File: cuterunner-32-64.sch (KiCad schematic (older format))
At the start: 39 parts

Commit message: Microcontroller part
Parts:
- added J?: Conn_02x06_Row_Letter_Last, symbol Connector_Generic:Conn_02x06_Row_Letter_Last
- added J?: Conn_01x05, symbol Connector_Generic:Conn_01x05
- C?: value C -> 0.1uF
- R?: value R -> 10k
- R?: value R -> 1k
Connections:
- net labels added: IFACE0, IFACE1, IFACE2, IFACE3, IFACE4, IFACE5, IFACE6, IFACE7, IFACE_CTRL0, IFACE_CTRL1, IFACE_CTRL2, IFACE_CTRL3, TCK_SWCLK, TDI_SWDIO, TDO, TMS_~RST, USB_N, USB_P
- wire segments 13 -> 44
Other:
- moved on the sheet: C?, R?

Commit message: Many CPLD parts
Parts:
- removed D? (x7): LED, symbol Device:LED
- removed R? (x10): R, symbol Device:R
- removed SW? (x3): SW_Push_Dual, symbol Switch:SW_Push_Dual
- added D? (x7): LED, symbol Device:LED
- added J? (x2): Conn_Coaxial, symbol Connector:Conn_Coaxial
- added J? (x2): Conn_01x03, symbol Connector_Generic:Conn_01x03
- added R? (x3): 10k, symbol Device:R
- added R? (x7): 1k, symbol Device:R
- added SW? (x3): SW_Push_Dual, symbol Switch:SW_Push_Dual
- C? (x4): value C -> 0.1uF
- R?: value R -> 1k
- R?: value R -> 10k
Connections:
- net labels added: BUT0, BUT1, BUT2, BUT3, CLK0, CLK1, CLK2, LED4, LED5, LED6, LED7, PMOD0, PMOD1, PMOD2, PMOD3, PMOD4, PMOD5, PMOD6, PMOD7
- wire segments 44 -> 173
- no-connect marks 1 -> 3
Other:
- moved on the sheet: C?, D?, J?, R?, SW?

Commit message: Added osc
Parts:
- added C?: 0.1uF, symbol Device:C
- added U?: OSC, symbol azonenberg-osc:OSC
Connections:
- wire segments 173 -> 178
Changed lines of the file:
@@
 Text Label 12250 4700 0    50   ~ 0
 CLK2
+$Comp
+L azonenberg-osc:OSC U?
+U 1 1 5E192FE7
+P 8600 4300
+F 0 "U?" H 8575 4587 60  0000 C CNN
+F 1 "OSC" H 8575 4481 60  0000 C CNN
+F 2 "" H 8600 4300 60  0000 C CNN
+F 3 "" H 8600 4300 60  0000 C CNN
+	1    8600 4300
+	1    0    0    -1
+$EndComp
+$Comp
+L Device:C C?
+U 1 1 5E193E24
+P 7600 4450
+F 0 "C?" H 7486 4404 50  0000 R CNN
+F 1 "0.1uF" H 7486 4495 50  0000 R CNN
+F 2 "" H 7638 4300 50  0001 C CNN
+F 3 "~" H 7600 4450 50  0001 C CNN
+	1    7600 4450
+	1    0    0    1
+$EndComp
+$Comp
+L power:+3V3 #PWR?
+U 1 1 5E19481A
+P 7600 4300
+F 0 "#PWR?" H 7600 4150 50  0001 C CNN
+F 1 "+3V3" H 7615 4473 50  0000 C CNN
+F 2 "" H 7600 4300 50  0001 C CNN
+F 3 "" H 7600 4300 50  0001 C CNN
+	1    7600 4300
+	1    0    0    -1
+$EndComp
+$Comp
+L power:GND #PWR?
+U 1 1 5E1951AF
+P 7600 4600
+F 0 "#PWR?" H 7600 4350 50  0001 C CNN
+F 1 "GND" H 7605 4427 50  0000 C CNN
+F 2 "" H 7600 4600 50  0001 C CNN
+F 3 "" H 7600 4600 50  0001 C CNN
+	1    7600 4600
+	1    0    0    -1
+$EndComp
+Wire Wire Line
+	7900 4500 7900 4600
+Wire Wire Line
+	7900 4600 7600 4600
+Connection ~ 7600 4600
+Wire Wire Line
+	7900 4400 7900 4300
+Wire Wire Line
+	7900 4300 7600 4300
+Connection ~ 7900 4300
+Connection ~ 7600 4300
+Wire Wire Line
+	9250 4300 9600 4300
+Text Label 9350 4300 0    50   ~ 0
+CLK0
 $EndSCHEMATC

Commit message: Schematic mostly done
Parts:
- added TP1: TestPoint, symbol Connector:TestPoint
- U5: renamed from U?; value OSC -> 50 MHz
- gave numbers to parts that had none: 46
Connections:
- wire segments 178 -> 179
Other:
- note added: "CPLD"
- note added: "Extra global clocks\n\nIntended use: populate only SMA *or* pin headers but not both"
- note added: "MCU programming/debug interface\n\nShares pins with CPLD JTAG, be careful"
- note added: "PMOD expansion (four pins shared with LEDs)"
- note added: "Power supplies"
- note added: "USB interface microcontroller\n\nIntended to be a parallel FIFO or UART interface to CPLD in addition to JTAG programming"
- note added: "User LEDs (four LEDs shared with PMOD)"
- note added: "User pushbuttons"
- moved on the sheet: C1, C2, C3, C4, C5, C6, C7, C8, C9, D1, D2, D3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

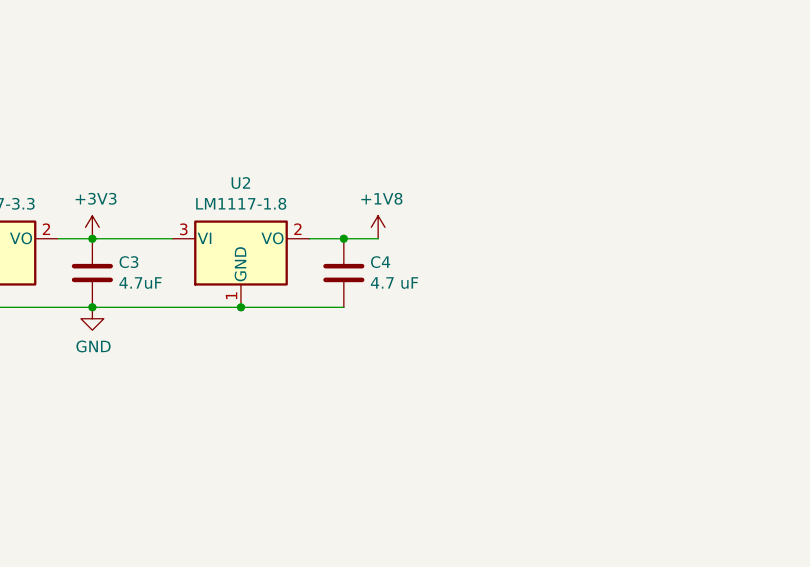
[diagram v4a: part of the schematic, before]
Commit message: Assign footprints
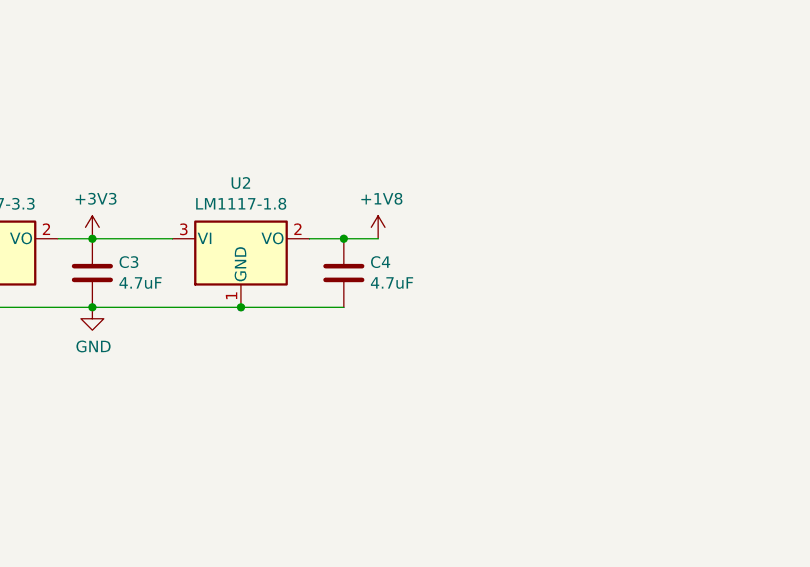
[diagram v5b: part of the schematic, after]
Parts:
- C1, C3: footprint (none) -> Capacitor_SMD:C_1206_3216Metric_Pad1.42x1.75mm_HandSolder
- C2, C5, C6, C7, C8, C9: footprint (none) -> Capacitor_SMD:C_0805_2012Metric_Pad1.15x1.40mm_HandSolder
- C4: value 4.7 uF -> 4.7uF; footprint (none) -> Capacitor_SMD:C_1206_3216Metric_Pad1.42x1.75mm_HandSolder
- D1, D2, D3, D4, D5, D6, D7, D8: footprint (none) -> LED_SMD:LED_0805_2012Metric_Pad1.15x1.40mm_HandSolder
- J1: footprint (none) -> Connector_PinHeader_2.54mm:PinHeader_1x05_P2.54mm_Vertical
- J2: footprint (none) -> Connector_PinHeader_2.54mm:PinHeader_2x06_P2.54mm_Horizontal
- J3, J5: footprint (none) -> azonenberg:CONN_SMA_PTH
- J4, J6: footprint (none) -> Connector_PinHeader_2.54mm:PinHeader_1x03_P2.54mm_Vertical
- R1, R10, R11, R12, R13, R14, R2, R3, R4, R5, R6, R7, R8, R9: footprint (none) -> Resistor_SMD:R_0805_2012Metric_Pad1.15x1.40mm_HandSolder
- SW1, SW2, SW3, SW4: footprint (none) -> Button_Switch_THT:SW_TH_Tactile_Omron_B3F-10xx
- TP1: footprint (none) -> Connector_PinHeader_2.54mm:PinHeader_1x01_P2.54mm_Vertical
- U1, U2: footprint (none) -> Package_TO_SOT_SMD:SOT-223-3_TabPin2
- U4: footprint (none) -> azonenberg:QFP_44_0.8MM
- U5: footprint (none) -> azonenberg:OSCILLATOR_3.2x2.5
- USB1: footprint (none) -> rqou:USB-MICRO-AB

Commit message: Placement of components
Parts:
- removed J2: Conn_02x06_Row_Letter_Last, Connector_PinHeader_2.54mm:PinHeader_2x06_P2.54mm_Horizontal, symbol Connector_Generic:Conn_02x06_Row_Letter_Last
- added J2: Conn_02x06_Odd_Even, Connector_PinHeader_2.54mm:PinHeader_2x06_P2.54mm_Horizontal, symbol Connector_Generic:Conn_02x06_Odd_Even
- added R15: 22, Resistor_SMD:R_0805_2012Metric_Pad1.15x1.40mm_HandSolder, symbol Device:R
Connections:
- wire segments 179 -> 180
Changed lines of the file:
@@
-	1    0    0    -1
-$EndComp
-$Comp
-L Connector_Generic:Conn_02x06_Row_Letter_Last J2
-U 1 1 5DFA98DA
-P 9600 9800
-F 0 "J2" H 9650 10217 50  0000 C CNN
-F 1 "Conn_02x06_Row_Letter_Last" H 9650 10126 50  0000 C CNN
-F 2 "Connector_PinHeader_2.54mm:PinHeader_2x06_P2.54mm_Horizontal" H 9600 9800 50  0001 C CNN
-F 3 "~" H 9600 9800 50  0001 C CNN
-	1    9600 9800
 	1    0    0    -1
 $EndComp
@@
 $EndComp
 Wire Wire Line
-	9400 10100 9900 10100
-Wire Wire Line
-	9900 10100 10000 10100
-Wire Wire Line
 	10000 10100 10000 9400
-Connection ~ 9900 10100
-Wire Wire Line
-	9900 10000 9400 10000
-Wire Wire Line
-	9400 10000 9300 10000
 Wire Wire Line
 	9300 10000 9300 10350
-Connection ~ 9400 10000
 Wire Wire Line
 	11400 6300 12050 6300
@@
 Connection ~ 12600 2100
 Connection ~ 12300 2100
-Wire Wire Line
-	13950 2100 14300 2100
-Text Label 14050 2100 0    50   ~ 0
+Text Label 14550 2100 0    50   ~ 0
 CLK0
 Wire Notes Line
@@
 Text Notes 550  600  0    50   ~ 0
 Power supplies
+$Comp
+L Device:R R15
+U 1 1 5DFC2966
+P 14200 2100
+F 0 "R15" V 13993 2100 50  0000 C CNN
+F 1 "22" V 14084 2100 50  0000 C CNN
+F 2 "Resistor_SMD:R_0805_2012Metric_Pad1.15x1.40mm_HandSolder" V 14130 2100 50  0001 C CNN
+F 3 "~" H 14200 2100 50  0001 C CNN
+	1    14200 2100
+	0    1    1    0
+$EndComp
+$Comp
+L Connector_Generic:Conn_02x06_Odd_Even J2
+U 1 1 5DFC5171
+P 9600 9800
+F 0 "J2" H 9650 10217 50  0000 C CNN
+F 1 "Conn_02x06_Odd_Even" H 9650 10126 50  0000 C CNN
+F 2 "Connector_PinHeader_2.54mm:PinHeader_2x06_P2.54mm_Horizontal" H 9600 9800 50  0001 C CNN
+F 3 "~" H 9600 9800 50  0001 C CNN
+	1    9600 9800
+	1    0    0    -1
+$EndComp
+Wire Wire Line
+	9300 10000 9400 10000
+Wire Wire Line
+	9900 10100 10000 10100
+Wire Wire Line
+	13950 2100 14050 2100
+Wire Wire Line
+	14350 2100 14850 2100
+Wire Wire Line
+	9900 10000 9400 10000
+Connection ~ 9400 10000
+Wire Wire Line
+	9400 10100 9900 10100
+Connection ~ 9900 10100
 $EndSCHEMATC

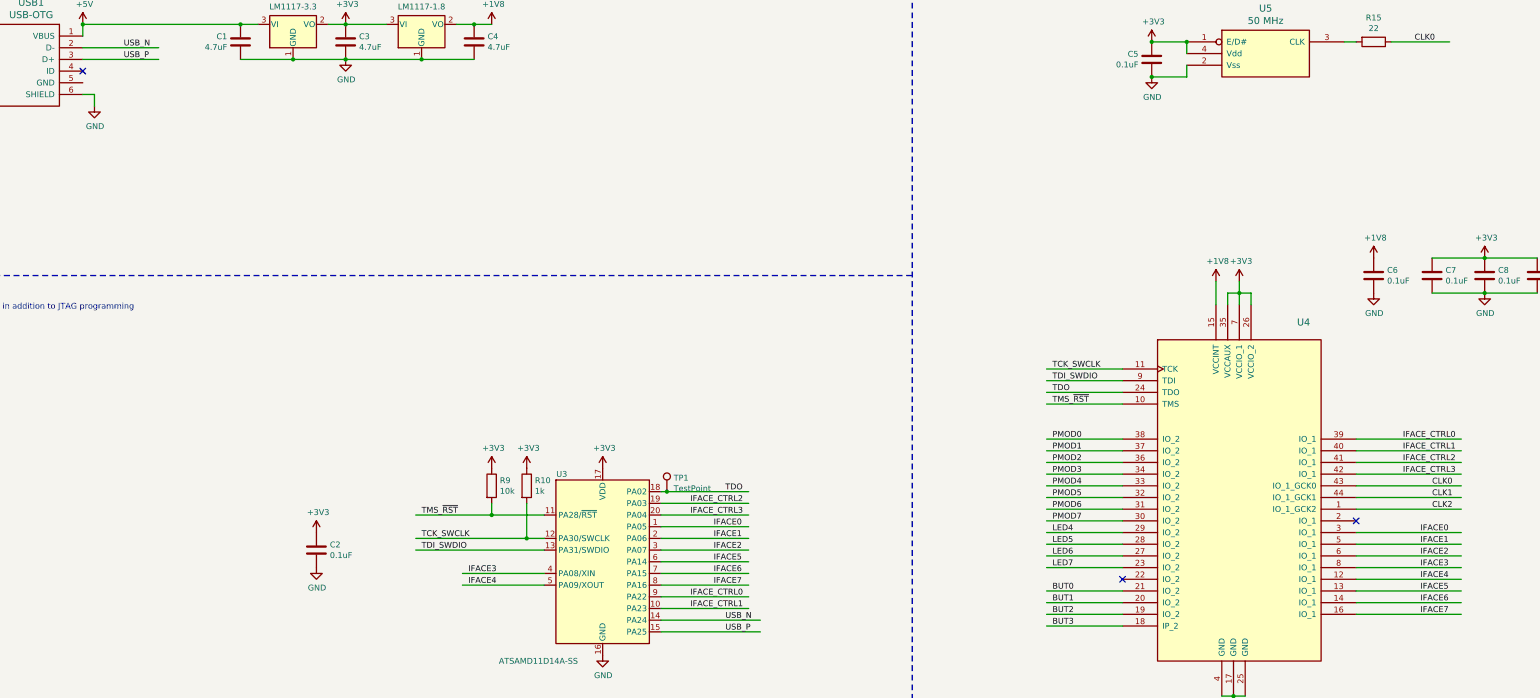
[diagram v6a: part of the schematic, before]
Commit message: Very sloppy first pass routing
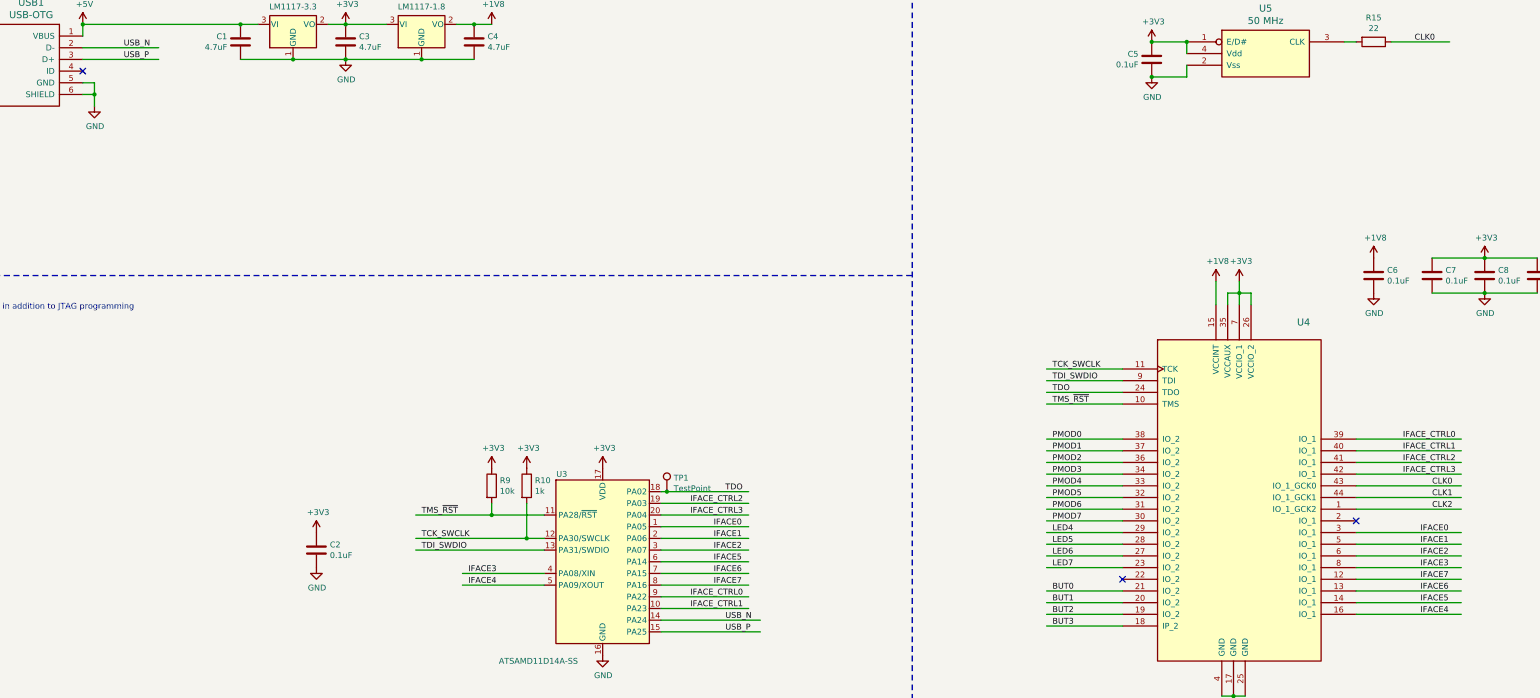
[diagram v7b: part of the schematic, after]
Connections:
- wire segments 180 -> 182
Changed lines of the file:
@@
 IFACE3
 Text Label 14600 6700 0    50   ~ 0
+IFACE7
+Text Label 14600 6800 0    50   ~ 0
+IFACE6
+Text Label 14600 6900 0    50   ~ 0
+IFACE5
+Text Label 14600 7000 0    50   ~ 0
 IFACE4
-Text Label 14600 6800 0    50   ~ 0
-IFACE5
-Text Label 14600 6900 0    50   ~ 0
-IFACE6
-Text Label 14600 7000 0    50   ~ 0
-IFACE7
 Text Label 14450 5500 0    50   ~ 0
 IFACE_CTRL0
@@
 	9400 10100 9900 10100
 Connection ~ 9900 10100
+Wire Wire Line
+	3150 2450 3250 2450
+Wire Wire Line
+	3250 2450 3250 2550
+Connection ~ 3250 2550
 $EndSCHEMATC
